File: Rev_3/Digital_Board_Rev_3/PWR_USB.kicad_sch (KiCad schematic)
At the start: 17 parts, among them J12 Barrel_Jack, Q1 BSS83P, U27 NCP1117-3.3_SOT223, U28 TC7662Bx0A

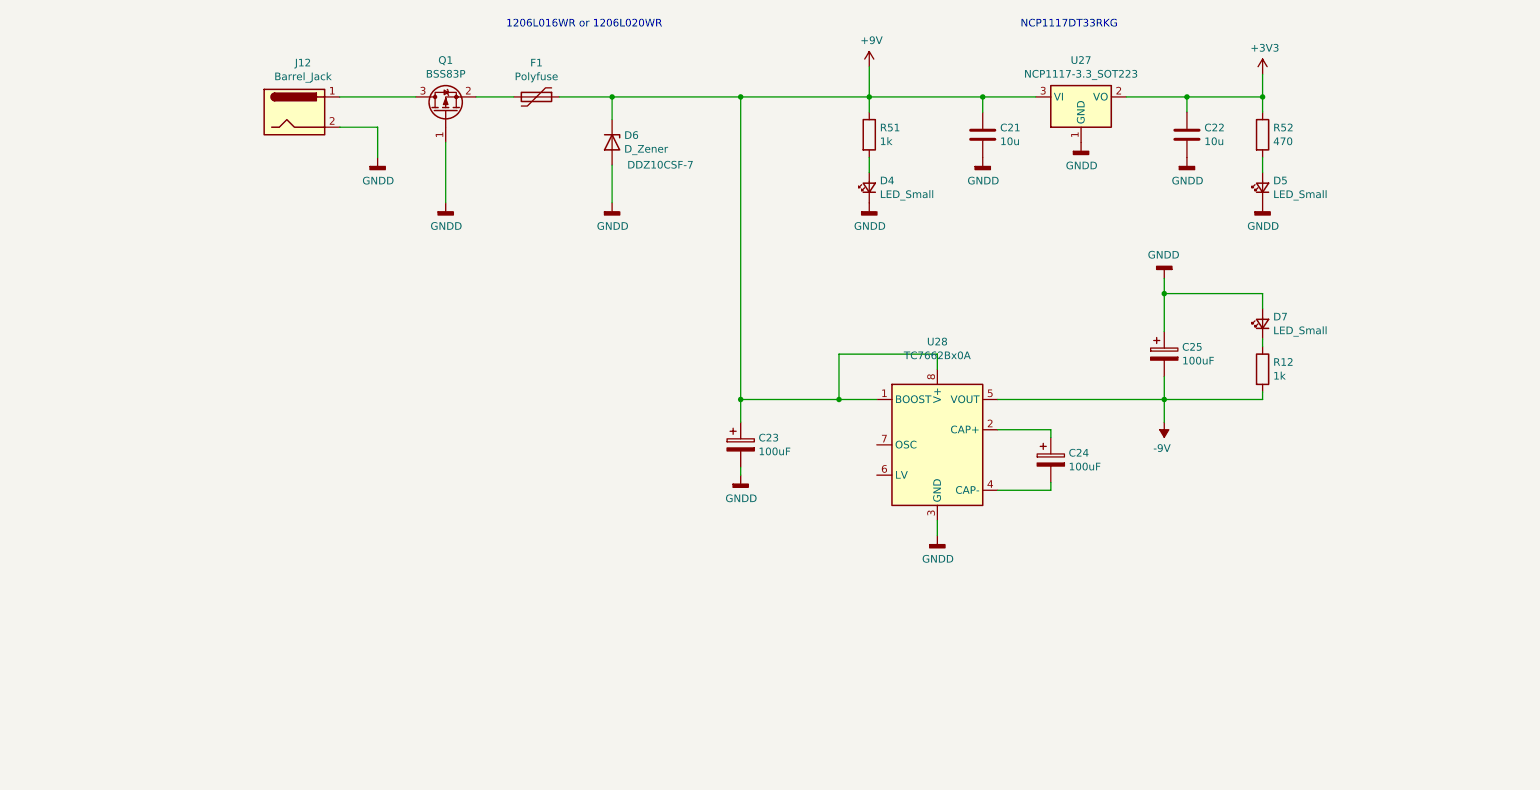
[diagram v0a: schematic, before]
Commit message: Pivoting to Passive Jack Boards
Finalized layout for input/output Jack Boards, which are now completely passive and connected with board-to-board connectors. Schematics are not updated yet, just figuring out placement/dimensions.
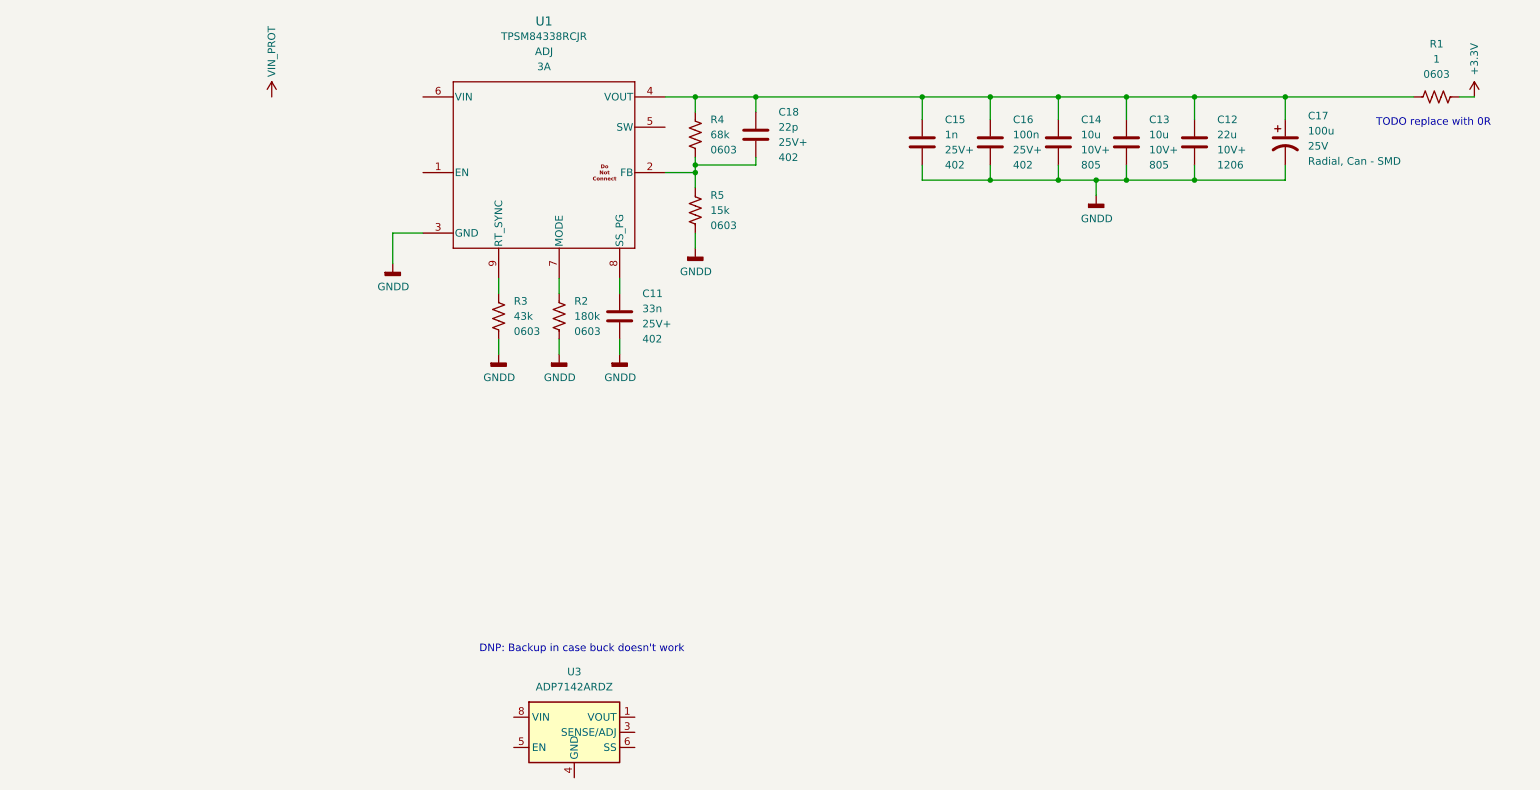
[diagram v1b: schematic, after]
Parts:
- removed C21, C22: 10u, Capacitor_SMD:C_1206_3216Metric_Pad1.33x1.80mm_HandSolder, symbol Device:C
- removed C23, C24, C25: 100uF, Capacitor_THT:CP_Radial_D5.0mm_P2.00mm, symbol Digital Board Rev 2-rescue:CP-Device
- removed D4, D5, D7: LED_Small, LED_SMD:LED_0805_2012Metric_Castellated, symbol Device:LED_Small
- removed D6: D_Zener, Diode_SMD:D_SMA_Handsoldering, symbol Device:D_Zener
- removed F1: Polyfuse, Fuse:Fuse_1206_3216Metric_Pad1.42x1.75mm_HandSolder, symbol Device:Polyfuse
- removed J12: Barrel_Jack, Connector_BarrelJack:BarrelJack_CUI_PJ-063AH_Horizontal_CircularHoles, symbol Connector:Barrel_Jack
- removed Q1: BSS83P, Package_TO_SOT_SMD:SOT-23, symbol Transistor_FET:BSS83P
- removed R12, R51: 1k, Resistor_SMD:R_0805_2012Metric_Pad1.20x1.40mm_HandSolder, symbol Device:R
- removed R52: 470, Resistor_SMD:R_0805_2012Metric_Pad1.20x1.40mm_HandSolder, symbol Device:R
- removed U27: NCP1117-3.3_SOT223, Package_TO_SOT_SMD:SOT-223-3_TabPin2, symbol Regulator_Linear:NCP1117-3.3_SOT223
- removed U28: TC7662Bx0A, Package_SO:SOIC-8_3.9x4.9mm_P1.27mm, symbol Converter_DCDC:TC7662Bx0A
- added C11: 33n, Capacitor_SMD:C_0402_1005Metric, symbol #gplm:cap/CAP-4003-033N
- added C12: 22u, Capacitor_SMD:C_1206_3216Metric, symbol #gplm:cap/CAP-4009-022U
- added C13, C14: 10u, Capacitor_SMD:C_0805:2012Metric, symbol #gplm:cap/CAP-4008-010U
- added C15: 1n, Capacitor_SMD:C_0402_1005Metric, symbol #gplm:cap/CAP-4001-001N
- added C16: 100n, Capacitor_SMD:C_0402_1005Metric, symbol #gplm:cap/CAP-4003-100N
- added C17: 100u, Capacitor_SMD:CP_Elec_8x6.2, symbol #gplm:cap/CAP-3005-100U
- added C18: 22p, Capacitor_SMD:C_0402_1005Metric, symbol #gplm:cap/CAP-4001-022P
- added R1: 1, Resistor_SMD:R_0603_1608Metric, symbol #gplm:res/RES-2001-001R
- added R2: 180k, Resistor_SMD:R_0603_1608Metric, symbol #gplm:res/RES-2001-180K
- added R3: 43k, Resistor_SMD:R_0603_1608Metric, symbol #gplm:res/RES-2001-043K
- added R4: 68k, Resistor_SMD:R_0603_1608Metric, symbol #gplm:res/RES-2001-068K
- added R5: 15k, Resistor_SMD:R_0603_1608Metric, symbol #gplm:res/RES-2001-015K
- added U1: TPSM84338RCJR, g-reg:TI-RCJ0009A-MFG, symbol #gplm:reg/REG-1003-001
- added U3: ADP7142ARDZ, Package_SO:SOIC-8-1EP_3.9x4.9mm_P1.27mm_EP2.29x3mm, symbol Regulator_Linear:ADP7142ARDZ
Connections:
- net GNDD: now also C11.2, C12.2, C13.2, C14.2, C15.2, C16.2, C17.2, R2.2, R3.2, R5.2, U1.3 (GND)
- new net: C12.1, C13.1, C14.1, C15.1, C16.1, C17.1, C18.1, R1.1, R4.1, U1.4 (VOUT)
- new net: C18.2, R4.2, R5.1, U1.2 (FB)
- new net: R3.1, U1.9 (RT_SYNC)
- new net: R2.1, U1.7 (MODE)
- new net: C11.1, U1.8 (SS_PG)
- new net: U3.1 (VOUT), U3.2 (VOUT)
- new net: U3.4 (GND), U3.9 (GND)
- new net: U3.7 (VIN), U3.8 (VIN)
- new net +3.3V: R1.2
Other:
- note added: "DNP: Backup in case buck doesn't work"
- note added: "TODO replace with 0R"
- note removed: "1206L016WR or 1206L020WR"
- note removed: "NCP1117DT33RKG"

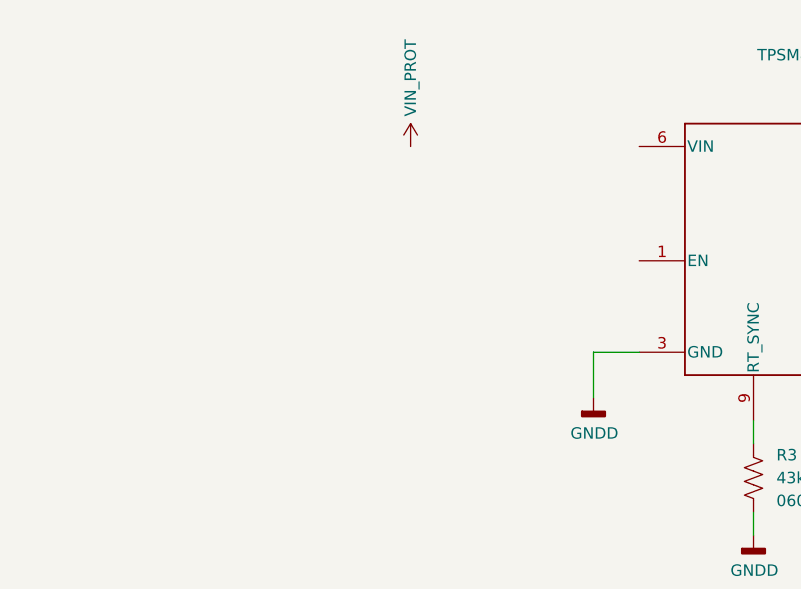
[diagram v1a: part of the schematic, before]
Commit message: Added analog board back, switched to Jacks on Bottom
Added analog board mezzanine back to fit everything. Finalized decision on jack boards; jacks on bottom, wire to board connectors between jack boards and digital board. Tentative board outlines defined and scoped out component placement.
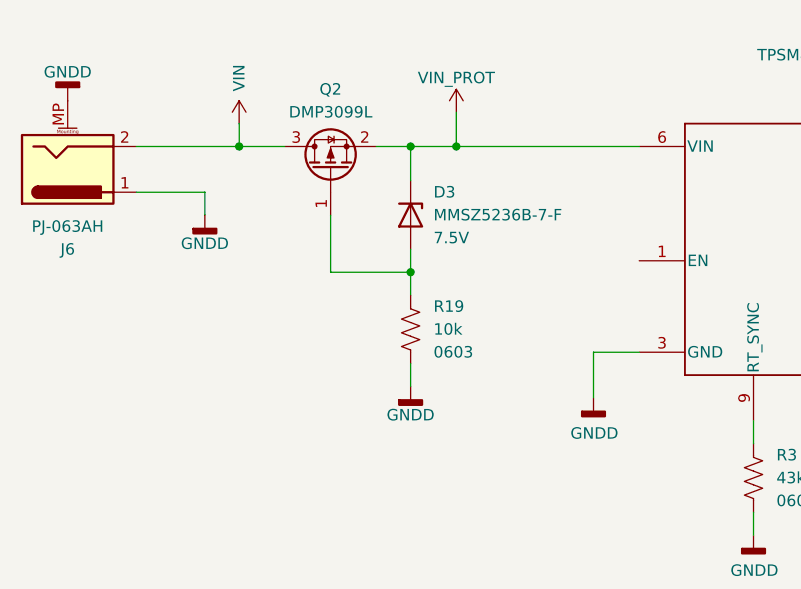
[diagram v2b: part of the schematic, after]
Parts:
- added D3: MMSZ5236B-7-F, Diode_SMD:D_SOD-123, symbol #gplm:zen/ZEN-0002-07V5
- added J6: 6, Connector_BarrelJack:BarrelJack_CUI_PJ-063AH_Horizontal, symbol #gplm:con/CON-1004-0001
- added Q2: DMP3099L, Package_TO_SOT_SMD:SOT-23, symbol #gplm:fet/XTR-1001-0001
- added R19: 10k, Resistor_SMD:R_0603_1608Metric, symbol #gplm:res/RES-2001-010K
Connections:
- net GNDD: now also J6.1, J6.MP (MountPin), R19.2
- net VIN_PROT: now also U1.6 (VIN), D3.1 (K), Q2.2 (S)
- new net: D3.2 (A), Q2.1 (G), R19.1
- new net VIN: J6.2, Q2.3 (D)
